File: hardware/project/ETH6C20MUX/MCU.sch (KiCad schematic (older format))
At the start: 32 parts, among them J601 Conn_02x05, J602 Conn_02x01, U601 S25FL064L_SOIC, U602 S25FL064L_SOIC, U603 STM32F765ZGT6, Y601 NX3225GD-8MHZ-STD-CRA-3

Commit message: Small updates in PCB design.
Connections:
- no-connect marks 74 -> 75
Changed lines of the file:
@@
 NoConn ~ 15150 6800
 NoConn ~ 15150 7300
+NoConn ~ 15150 5100
 $EndSCHEMATC

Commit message: Software development. SPI flash write/read works correctly.
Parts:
- U601, U602: value S25FL064L_SOIC -> S25FL064L
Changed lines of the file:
@@
 EESchema Schematic File Version 4
-LIBS:ETH6C20MUX-cache
 EELAYER 30 0
 EELAYER END
@@
 P 1650 3300
 F 0 "U601" H 1650 3865 50  0000 C CNN
-F 1 "S25FL064L_SOIC" H 1650 3774 50  0000 C CNN
+F 1 "S25FL064L" H 1650 3774 50  0000 C CNN
 F 2 "Package_SO:SOIC-8_5.23x5.23mm_P1.27mm" H 1900 3900 50  0001 C CNN
 F 3 "" H 1900 3900 50  0001 C CNN
@@
 P 1650 4650
 F 0 "U602" H 1650 5215 50  0000 C CNN
-F 1 "S25FL064L_SOIC" H 1650 5124 50  0000 C CNN
+F 1 "S25FL064L" H 1650 5124 50  0000 C CNN
 F 2 "Package_SO:SOIC-8_5.23x5.23mm_P1.27mm" H 1900 5250 50  0001 C CNN
 F 3 "" H 1900 5250 50  0001 C CNN

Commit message: PCB redesign
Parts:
- added D601: RED, LED_SMD:LED_0603_1608Metric_Pad1.05x0.95mm_HandSolder, symbol Device:LED
- added D602: GREEN, LED_SMD:LED_0603_1608Metric_Pad1.05x0.95mm_HandSolder, symbol Device:LED
- added D603: BLUE, LED_SMD:LED_0603_1608Metric_Pad1.05x0.95mm_HandSolder, symbol Device:LED
- added R602, R603, R605: 680, Resistor_SMD:R_0603_1608Metric_Pad0.98x0.95mm_HandSolder, symbol Device:R
- added RN601: 10k, Resistor_SMD:R_Array_Convex_5x0603, symbol Device:R_Pack05_Split
- added SW601: A6SN-5104, Button_Switch_SMD:SW_DIP_SPSTx05_Slide_6.7x14.26mm_W8.61mm_P2.54mm_LowProfile, symbol Switch:SW_DIP_x05
- C601, C602, C603, C604, C607, C608, C609, C610, C611, C612, C613, C614, C615, C616, C617, C618, C619, C620, C621: footprint Capacitor_SMD:C_0603_1608Metric_Pad1.05x0.95mm_HandSolder -> Capacitor_SMD:C_0603_1608Metric_Pad1.08x0.95mm_HandSolder
- R601, R604, R608, R609: footprint Resistor_SMD:R_0603_1608Metric_Pad1.05x0.95mm_HandSolder -> Resistor_SMD:R_0603_1608Metric_Pad0.98x0.95mm_HandSolder
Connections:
- net +3V3: now also D601.2 (A), D602.2 (A), D603.2 (A), RN601.10 (R1.2), RN601.6 (R5.2), RN601.7 (R4.2), RN601.8 (R3.2), RN601.9 (R2.2)
- net GND: now also SW601.1, SW601.2, SW601.3, SW601.4, SW601.5
- net ETH_CODE4: now reaches U603.74 (PB13,TIM1_CH1N,SPI2_SCK,I2S2_CK,DFSDM1_CKIN1,USART3_CTS,UART5_TX,CAN2_TX,OTG_HS_ULPI_D6,ETH_MII_TXD1,ETH_RMII_TXD1,EVENTOUT,OTG_HS_VBUS)
- net ETH_CODE4: now also RN601.5 (R5.1), SW601.6
- net ETH_CODE3: now reaches U603.75 (PB14,TIM1_CH2N,TIM8_CH2N,USART1_TX,SPI2_MISO,DFSDM1_DATIN2,USART3_RTS,UART4_RTS,TIM12_CH1,SDMMC2_D0,OTG_HS_DM,EVENTOUT)
- net ETH_CODE3: now also RN601.4 (R4.1), SW601.7
- net ETH_CODE2: now reaches U603.76 (PB15,RTC_REFIN,TIM1_CH3N,TIM8_CH3N,USART1_RX,SPI2_MOSI,I2S2_SD,DFSDM1_CKIN2,UART4_CTS,TIM12_CH2,SDMMC2_D1,OTG_HS_DP,EVENTOUT)
- net ETH_CODE2: now also RN601.3 (R3.1), SW601.8
- net ETH_CODE1: now reaches U603.77 (PD8,DFSDM1_CKIN3,USART3_TX,SPDIF_RX1,FMC_D13,EVENTOUT)
- net ETH_CODE1: now also RN601.2 (R2.1), SW601.9
- net ETH_CODE0: now reaches U603.78 (PD9,DFSDM1_DATIN3,USART3_RX,FMC_D14,EVENTOUT)
- net ETH_CODE0: now also RN601.1 (R1.1), SW601.10
- net at U603.80 (PD11,I2C4_SMBA,USART3_CTS,QUADSPI_BK1_IO0,SAI2_SD_A,FMC_A16,FMC_CLE,EVENTOUT): now also R602.2
- net at U603.81 (PD12,TIM4_CH1,LPTIM1_IN1,I2C4_SCL,USART3_RTS,QUADSPI_BK1_IO1,SAI2_FS_A,FMC_A17,FMC_ALE,EVENTOUT): now also R603.2
- net at U603.82 (PD13,TIM4_CH2,LPTIM1_OUT,I2C4_SDA,QUADSPI_BK1_IO3,SAI2_SCK_A,FMC_A18,EVENTOUT): now also R605.2
- new net: D601.1 (K), R602.1
- new net: D602.1 (K), R603.1
- new net: D603.1 (K), R605.1
- no-connect marks 75 -> 67
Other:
- moved on the sheet: C601, C602, C603, C604, C605, C606, C607, C608, J601, R601, R604, R608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

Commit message: PCB design
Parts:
- D601, D602, D603: footprint LED_SMD:LED_0603_1608Metric_Pad1.05x0.95mm_HandSolder -> LED_SMD:LED_Dialight_591
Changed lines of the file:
@@
 F 0 "D601" H 15550 3550 50  0000 C CNN
 F 1 "RED" H 15750 3350 50  0000 C CNN
-F 2 "LED_SMD:LED_0603_1608Metric_Pad1.05x0.95mm_HandSolder" H 15550 3450 50  0001 C CNN
+F 2 "LED_SMD:LED_Dialight_591" H 15550 3450 50  0001 C CNN
 F 3 "~" H 15550 3450 50  0001 C CNN
 	1    15550 3450
@@
 F 0 "D602" H 15550 3800 50  0000 C CNN
 F 1 "GREEN" H 15700 3600 50  0000 C CNN
-F 2 "LED_SMD:LED_0603_1608Metric_Pad1.05x0.95mm_HandSolder" H 15550 3700 50  0001 C CNN
+F 2 "LED_SMD:LED_Dialight_591" H 15550 3700 50  0001 C CNN
 F 3 "~" H 15550 3700 50  0001 C CNN
 	1    15550 3700
@@
 F 0 "D603" H 15550 4100 50  0000 C CNN
 F 1 "BLUE" H 15700 3900 50  0000 C CNN
-F 2 "LED_SMD:LED_0603_1608Metric_Pad1.05x0.95mm_HandSolder" H 15550 4000 50  0001 C CNN
+F 2 "LED_SMD:LED_Dialight_591" H 15550 4000 50  0001 C CNN
 F 3 "~" H 15550 4000 50  0001 C CNN
 	1    15550 4000

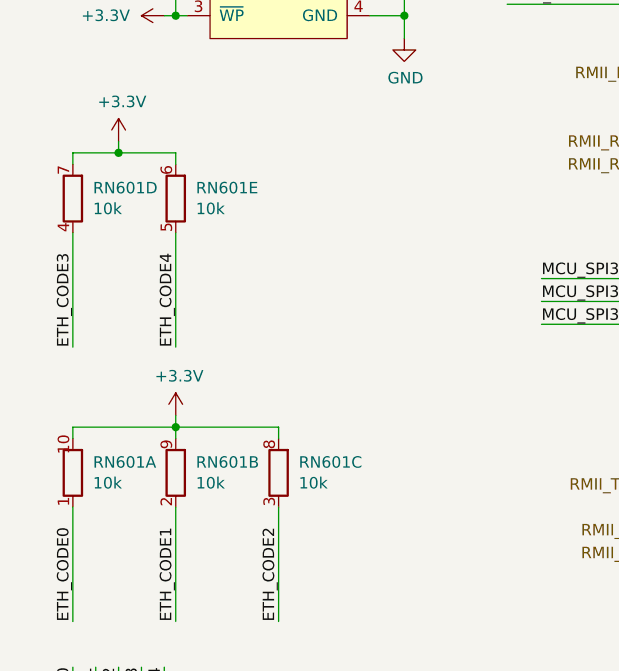
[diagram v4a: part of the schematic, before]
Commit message: PCB main and module layout.
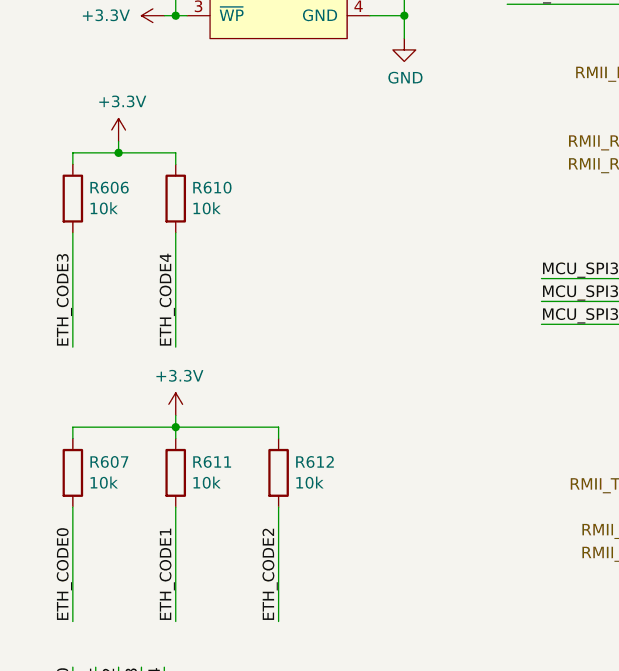
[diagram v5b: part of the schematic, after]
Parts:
- removed RN601: 10k, Resistor_SMD:R_Array_Convex_5x0603, symbol Device:R_Pack05_Split
- added R606, R607, R610, R611, R612: 10k, Resistor_SMD:R_0603_1608Metric_Pad0.98x0.95mm_HandSolder, symbol Device:R
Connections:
- net +3V3: now also R606.1, R607.1, R610.1, R611.1, R612.1
- net ETH_CODE0: now also R607.2
- net ETH_CODE1: now also R611.2
- net ETH_CODE2: now also R612.2
- net ETH_CODE3: now also R606.2
- net ETH_CODE4: now also R610.2
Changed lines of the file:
@@
 	1000 5450 1250 5450
-$Comp
-L Device:R_Pack05_Split RN601
-U 1 1 612A41F8
-P 800 6850
-F 0 "RN601" H 888 6896 50  0000 L CNN
-F 1 "10k" H 888 6805 50  0000 L CNN
-F 2 "Resistor_SMD:R_Array_Convex_5x0603" V 720 6850 50  0001 C CNN
-F 3 "~" H 800 6850 50  0001 C CNN
-	1    800  6850
-	1    0    0    -1
-$EndComp
-$Comp
-L Device:R_Pack05_Split RN601
-U 2 1 612A6686
-P 1250 6850
-F 0 "RN601" H 1338 6896 50  0000 L CNN
-F 1 "10k" H 1338 6805 50  0000 L CNN
-F 2 "Resistor_SMD:R_Array_Convex_5x0603" V 1170 6850 50  0001 C CNN
-F 3 "~" H 1250 6850 50  0001 C CNN
-	2    1250 6850
-	1    0    0    -1
-$EndComp
-$Comp
-L Device:R_Pack05_Split RN601
-U 5 1 612A70CB
-P 1250 5650
-F 0 "RN601" H 1338 5696 50  0000 L CNN
-F 1 "10k" H 1338 5605 50  0000 L CNN
-F 2 "Resistor_SMD:R_Array_Convex_5x0603" V 1170 5650 50  0001 C CNN
-F 3 "~" H 1250 5650 50  0001 C CNN
-	5    1250 5650
-	1    0    0    -1
-$EndComp
-$Comp
-L Device:R_Pack05_Split RN601
-U 3 1 612A7CAB
-P 1700 6850
-F 0 "RN601" H 1788 6896 50  0000 L CNN
-F 1 "10k" H 1788 6805 50  0000 L CNN
-F 2 "Resistor_SMD:R_Array_Convex_5x0603" V 1620 6850 50  0001 C CNN
-F 3 "~" H 1700 6850 50  0001 C CNN
-	3    1700 6850
-	1    0    0    -1
-$EndComp
-$Comp
-L Device:R_Pack05_Split RN601
-U 4 1 612A89FB
-P 800 5650
-F 0 "RN601" H 888 5696 50  0000 L CNN
-F 1 "10k" H 888 5605 50  0000 L CNN
-F 2 "Resistor_SMD:R_Array_Convex_5x0603" V 720 5650 50  0001 C CNN
-F 3 "~" H 800 5650 50  0001 C CNN
-	4    800  5650
-	1    0    0    -1
-$EndComp
 $Comp
 L Device:R R602
@@
 	15850 3400 15850 3450
 Connection ~ 15850 3450
+$Comp
+L Device:R R606
+U 1 1 6032A162
+P 800 5650
+F 0 "R606" H 870 5696 50  0000 L CNN
+F 1 "10k" H 870 5605 50  0000 L CNN
+F 2 "Resistor_SMD:R_0603_1608Metric_Pad0.98x0.95mm_HandSolder" V 730 5650 50  0001 C CNN
+F 3 "~" H 800 5650 50  0001 C CNN
+	1    800  5650
+	1    0    0    -1
+$EndComp
+$Comp
+L Device:R R610
+U 1 1 6032BA69
+P 1250 5650
+F 0 "R610" H 1320 5696 50  0000 L CNN
+F 1 "10k" H 1320 5605 50  0000 L CNN
+F 2 "Resistor_SMD:R_0603_1608Metric_Pad0.98x0.95mm_HandSolder" V 1180 5650 50  0001 C CNN
+F 3 "~" H 1250 5650 50  0001 C CNN
+	1    1250 5650
+	1    0    0    -1
+$EndComp
+$Comp
+L Device:R R607
+U 1 1 6032C32C
+P 800 6850
+F 0 "R607" H 870 6896 50  0000 L CNN
+F 1 "10k" H 870 6805 50  0000 L CNN
+F 2 "Resistor_SMD:R_0603_1608Metric_Pad0.98x0.95mm_HandSolder" V 730 6850 50  0001 C CNN
+F 3 "~" H 800 6850 50  0001 C CNN
+	1    800  6850
+	1    0    0    -1
+$EndComp
+$Comp
+L Device:R R611
+U 1 1 6032C8D3
+P 1250 6850
+F 0 "R611" H 1320 6896 50  0000 L CNN
+F 1 "10k" H 1320 6805 50  0000 L CNN
+F 2 "Resistor_SMD:R_0603_1608Metric_Pad0.98x0.95mm_HandSolder" V 1180 6850 50  0001 C CNN
+F 3 "~" H 1250 6850 50  0001 C CNN
+	1    1250 6850
+	1    0    0    -1
+$EndComp
+$Comp
+L Device:R R612
+U 1 1 6032CB6A
+P 1700 6850
+F 0 "R612" H 1770 6896 50  0000 L CNN
+F 1 "10k" H 1770 6805 50  0000 L CNN
+F 2 "Resistor_SMD:R_0603_1608Metric_Pad0.98x0.95mm_HandSolder" V 1630 6850 50  0001 C CNN
+F 3 "~" H 1700 6850 50  0001 C CNN
+	1    1700 6850
+	1    0    0    -1
+$EndComp
 $EndSCHEMATC

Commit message: PCB modifications.
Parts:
- removed R606, R607, R610, R611, R612: 10k, Resistor_SMD:R_0603_1608Metric_Pad0.98x0.95mm_HandSolder, symbol Device:R
- removed SW601: A6SN-5104, Button_Switch_SMD:SW_DIP_SPSTx05_Slide_6.7x14.26mm_W8.61mm_P2.54mm_LowProfile, symbol Switch:SW_DIP_x05
- renumbered R605 to R604, R604 to R605, R608 to R606, R609 to R607
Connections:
- net ETH_CODE0: no longer names the net of U603.78 (PD9,DFSDM1_DATIN3,USART3_RX,FMC_D14,EVENTOUT)
- net ETH_CODE1: no longer names the net of U603.77 (PD8,DFSDM1_CKIN3,USART3_TX,SPDIF_RX1,FMC_D13,EVENTOUT)
- net ETH_CODE2: no longer names the net of U603.76 (PB15,RTC_REFIN,TIM1_CH3N,TIM8_CH3N,USART1_RX,SPI2_MOSI,I2S2_SD,DFSDM1_CKIN2,UART4_CTS,TIM12_CH2,SDMMC2_D1,OTG_HS_DP,EVENTOUT)
- net ETH_CODE3: no longer names the net of U603.75 (PB14,TIM1_CH2N,TIM8_CH2N,USART1_TX,SPI2_MISO,DFSDM1_DATIN2,USART3_RTS,UART4_RTS,TIM12_CH1,SDMMC2_D0,OTG_HS_DM,EVENTOUT)
- net ETH_CODE4: no longer names the net of U603.74 (PB13,TIM1_CH1N,SPI2_SCK,I2S2_CK,DFSDM1_CKIN1,USART3_CTS,UART5_TX,CAN2_TX,OTG_HS_ULPI_D6,ETH_MII_TXD1,ETH_RMII_TXD1,EVENTOUT,OTG_HS_VBUS)
- no-connect marks 67 -> 72
